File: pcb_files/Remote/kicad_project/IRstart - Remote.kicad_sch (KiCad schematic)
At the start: 44 parts, among them SW1 SW_DIP_x02, SW2 SW_DIP_x02, SW3 SW_DPDT_x2

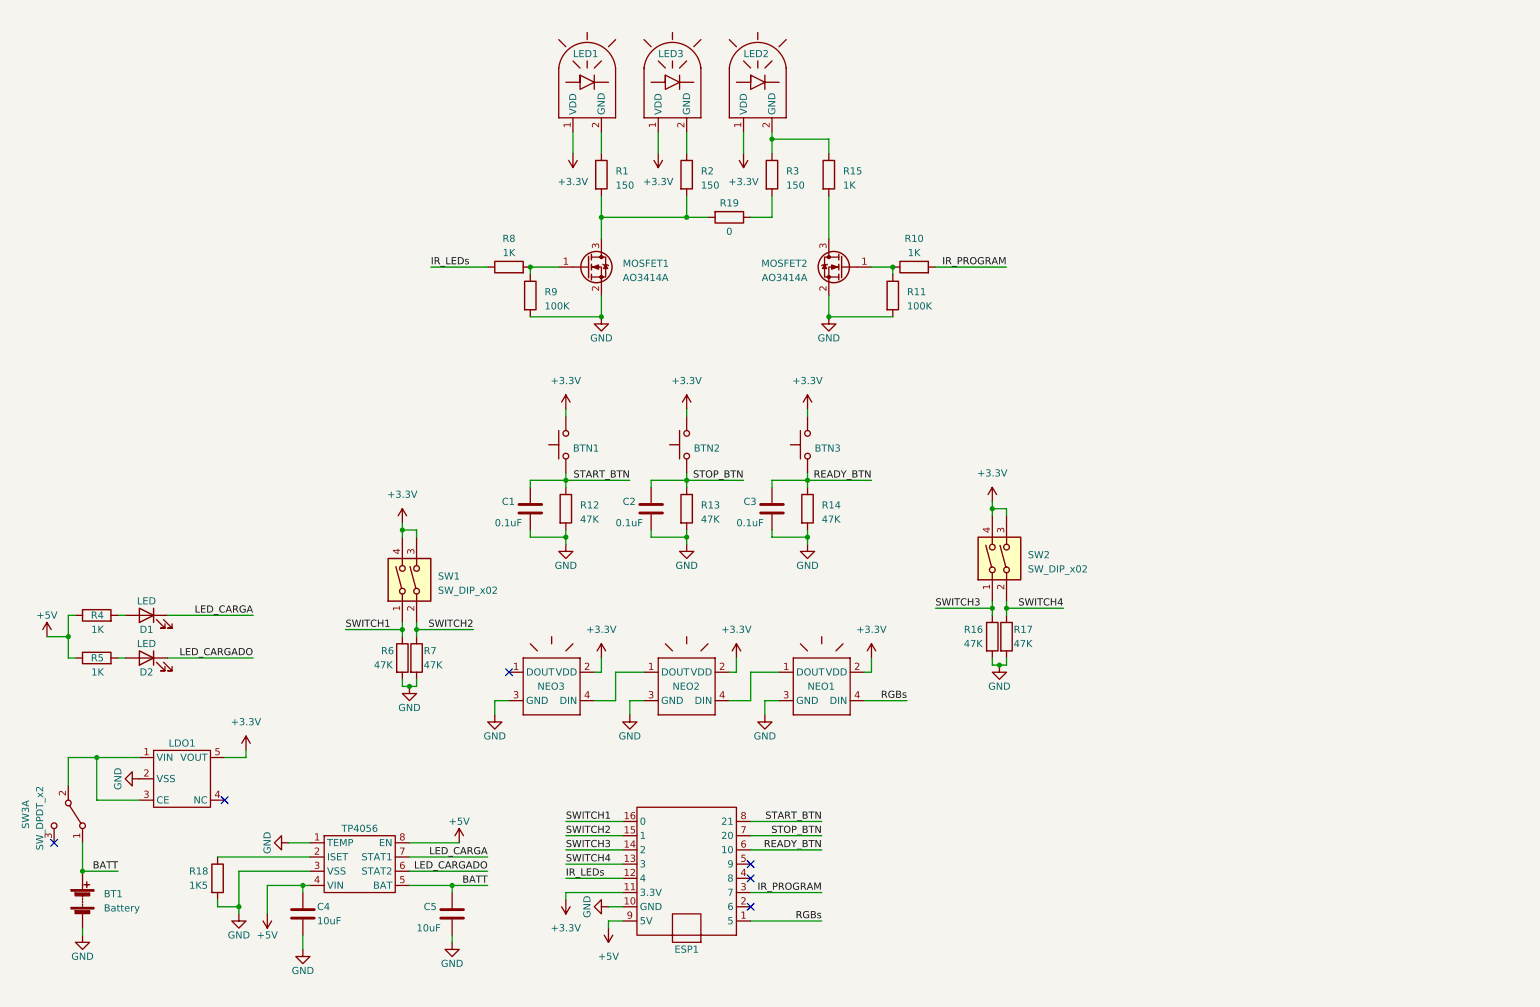
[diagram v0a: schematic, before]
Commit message: Añade gerbers de remote y adecenta el esquematico
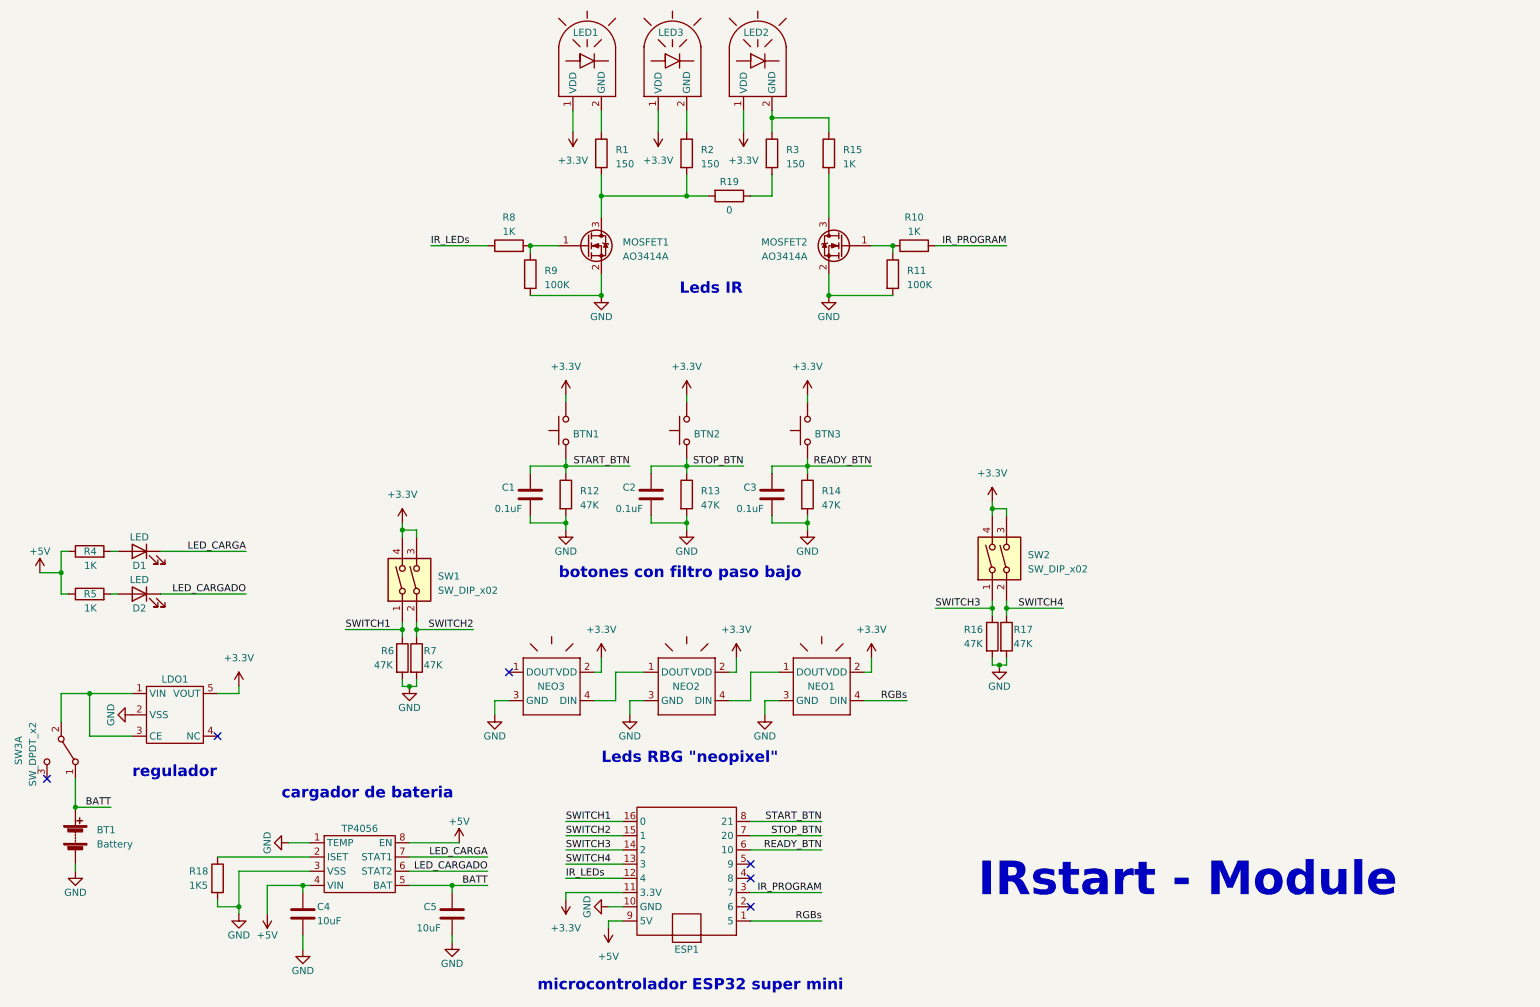
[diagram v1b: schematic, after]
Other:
- note added: "IRstart - Module"
- note added: "Leds IR"
- note added: "Leds RBG "neopixel""
- note added: "botones con filtro paso bajo"
- note added: "cargador de bateria"
- note added: "microcontrolador ESP32 super mini"
- note added: "regulador"
- moved on the sheet: BT1, BTN1, BTN2, BTN3, C1, C2, C3, D1, D2, LDO1, LED1, LED2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

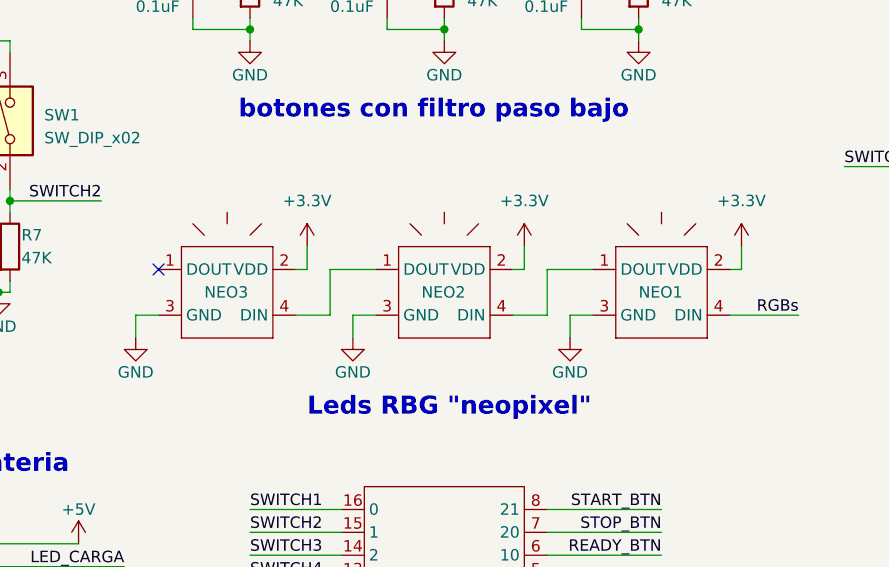
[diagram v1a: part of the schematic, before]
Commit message: Corrige leds RGB con huella incorrecta
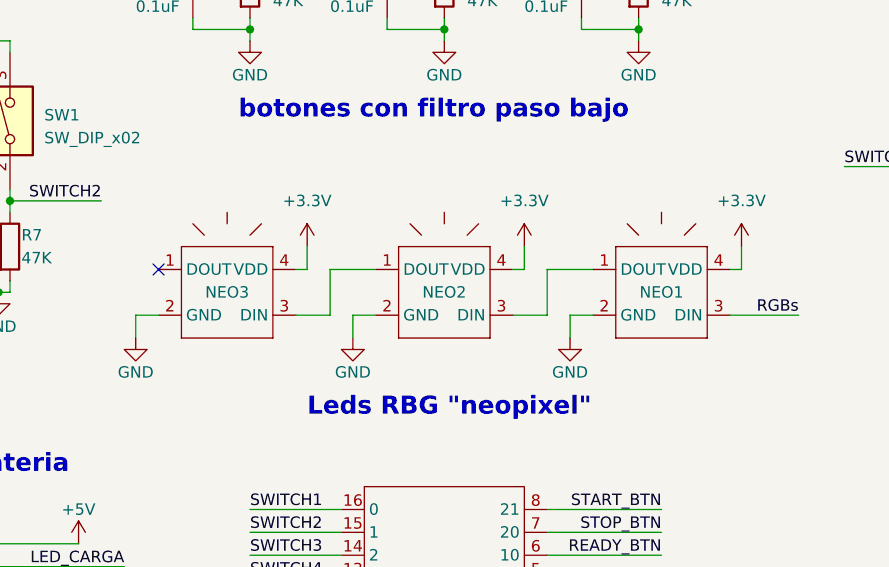
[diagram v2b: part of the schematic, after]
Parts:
- removed NEO1, NEO2, NEO3: ~, custom_footprints:LED_WS2812B_2.0x2.0mm, symbol custom_symbols:Led_5mm_WS2812D_
- added NEO1, NEO2, NEO3: ~, custom_footprints:LED_WS2812B_2.0x2.0mm, symbol custom_symbols:2020_Neopixel
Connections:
- net +3.3V: now also NEO1.4 (VDD), NEO2.4 (VDD), NEO3.4 (VDD)
- net GND: now also NEO1.2 (GND), NEO2.2 (GND), NEO3.2 (GND)
- net RGBs: now also NEO1.3 (DIN)
- new net: NEO1.1 (DOUT), NEO2.3 (DIN)
- new net: NEO2.1 (DOUT), NEO3.3 (DIN)
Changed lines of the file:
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@@
-    )
-  )
-  (symbol (lib_name "Led_5mm_WS2812D__1") (lib_id "custom_symbols:Led_5mm_WS2812D_") (at 139.7 143.51 0) (unit 1)
-    (in_bom yes) (on_board yes) (dnp no)
-    (property "Reference" "NEO2" (at 139.7 139.7 0)
-      (effects (font (size 1.27 1.27)) (justify left))
-    )
-    (property "Value" "~" (at 142.24 133.35 0)
-      (effects (font (size 1.27 1.27)))
-    )
-    (property "Footprint" "custom_footprints:LED_WS2812B_2.0x2.0mm" (at 142.24 147.32 0)
-      (effects (font (size 1.27 1.27)) hide)
-    )
-    (property "Datasheet" "" (at 139.7 143.51 0)
-      (effects (font (size 1.27 1.27)) hide)
-    )
-    (property "Aliexpress" "https://es.aliexpress.com/item/1005006449117605.html" (at 139.7 143.51 0)
-      (effects (font (size 1.27 1.27)) hide)
-    )
-    (pin "1")
-    (pin "2")
-    (pin "3")
-    (pin "4")
-    (instances
-      (project "IRstart - Remote"
-        (path "/1b43c11f-8fb9-449e-8aa5-32f4fc7dc112"
-          (reference "NEO2") (unit 1)
-        )
-      )
-      (project "PX-CORE"
-        (path "/b9d93021-acc9-4fa4-951b-65a13734b94e"
-          (reference "LED3") (unit 1)
-        )
-      )
     )
   )
@@
         (path "/b9d93021-acc9-4fa4-951b-65a13734b94e"
           (reference "#PWR018") (unit 1)
-        )
-      )
-    )
-  )
-  (symbol (lib_name "Led_5mm_WS2812D__1") (lib_id "custom_symbols:Led_5mm_WS2812D_") (at 163.83 143.51 0) (unit 1)
-    (in_bom yes) (on_board yes) (dnp no)
-    (property "Reference" "NEO1" (at 163.83 139.7 0)
-      (effects (font (size 1.27 1.27)) (justify left))
-    )
-    (property "Value" "~" (at 166.37 133.35 0)
-      (effects (font (size 1.27 1.27)))
-    )
-    (property "Footprint" "custom_footprints:LED_WS2812B_2.0x2.0mm" (at 166.37 147.32 0)
-      (effects (font (size 1.27 1.27)) hide)
-    )
-    (property "Datasheet" "" (at 163.83 143.51 0)
-      (effects (font (size 1.27 1.27)) hide)
-    )
-    (property "Aliexpress" "https://es.aliexpress.com/item/1005006449117605.html" (at 163.83 143.51 0)
-      (effects (font (size 1.27 1.27)) hide)
-    )
-    (pin "1")
-    (pin "2")
-    (pin "3")
-    (pin "4")
-    (instances
-      (project "IRstart - Remote"
-        (path "/1b43c11f-8fb9-449e-8aa5-32f4fc7dc112"
-          (reference "NEO1") (unit 1)
-        )
-      )
-      (project "PX-CORE"
-        (path "/b9d93021-acc9-4fa4-951b-65a13734b94e"
-          (reference "LED3") (unit 1)
         )
       )
@@
     )
   )
+  (symbol (lib_id "custom_symbols:2020_Neopixel") (at 163.83 143.51 0) (unit 1)
+    (in_bom yes) (on_board yes) (dnp no)
+    (property "Reference" "NEO1" (at 166.37 139.7 0)
+      (effects (font (size 1.27 1.27)))
+    )
+    (property "Value" "~" (at 166.37 133.35 0)
+      (effects (font (size 1.27 1.27)))
+    )
+    (property "Footprint" "custom_footprints:LED_WS2812B_2.0x2.0mm" (at 166.37 147.32 0)
+      (effects (font (size 1.27 1.27)) hide)
+    )
+    (property "Datasheet" "" (at 163.83 143.51 0)
+      (effects (font (size 1.27 1.27)) hide)
+    )
+    (property "Aliexpress" "https://es.aliexpress.com/item/1005006449117605.html" (at 163.83 143.51 0)
+      (effects (font (size 1.27 1.27)) hide)
+    )
+    (pin "1")
+    (pin "2")
+    (pin "3")
+    (pin "4")
+    (instances
+      (project "IRstart - Remote"
+        (path "/1b43c11f-8fb9-449e-8aa5-32f4fc7dc112"
+          (reference "NEO1") (unit 1)
+        )
+      )
+    )
+  )
   (symbol (lib_id "power:+5V") (at 67.31 180.34 180) (unit 1)
     (in_bom yes) (on_board yes) (dnp no)
@@
     )
   )
-  (symbol (lib_name "Led_5mm_WS2812D__1") (lib_id "custom_symbols:Led_5mm_WS2812D_") (at 115.57 143.51 0) (unit 1)
-    (in_bom yes) (on_board yes) (dnp no)
-    (property "Reference" "NEO3" (at 115.57 139.7 0)
-      (effects (font (size 1.27 1.27)) (justify left))
+  (symbol (lib_id "custom_symbols:2020_Neopixel") (at 115.57 143.51 0) (unit 1)
+    (in_bom yes) (on_board yes) (dnp no)
+    (property "Reference" "NEO3" (at 118.11 139.7 0)
+      (effects (font (size 1.27 1.27)))
     )
     (property "Value" "~" (at 118.11 133.35 0)
@@
         (path "/1b43c11f-8fb9-449e-8aa5-32f4fc7dc112"
           (reference "NEO3") (unit 1)
-        )
-      )
-      (project "PX-CORE"
-        (path "/b9d93021-acc9-4fa4-951b-65a13734b94e"
-          (reference "LED3") (unit 1)
         )
       )
@@
         )
       )
+    )
+  )
+  (symbol (lib_id "custom_symbols:2020_Neopixel") (at 139.7 143.51 0) (unit 1)
+    (in_bom yes) (on_board yes) (dnp no)
+    (property "Reference" "NEO2" (at 142.24 139.7 0)
+      (effects (font (size 1.27 1.27)))
+    )
+    (property "Value" "~" (at 142.24 133.35 0)
+      (effects (font (size 1.27 1.27)))
+    )
+    (property "Footprint" "custom_footprints:LED_WS2812B_2.0x2.0mm" (at 142.24 147.32 0)
+      (effects (font (size 1.27 1.27)) hide)
+    )
+    (property "Datasheet" "" (at 139.7 143.51 0)
+      (effects (font (size 1.27 1.27)) hide)
+    )
+    (property "Aliexpress" "https://es.aliexpress.com/item/1005006449117605.html" (at 139.7 143.51 0)
+      (effects (font (size 1.27 1.27)) hide)
+    )
+    (pin "1")
+    (pin "2")
+    (pin "3")
+    (pin "4")
+    (instances
+      (project "IRstart - Remote"
+        (path "/1b43c11f-8fb9-449e-8aa5-32f4fc7dc112"
+          (reference "NEO2") (unit 1)
+        )
+      )

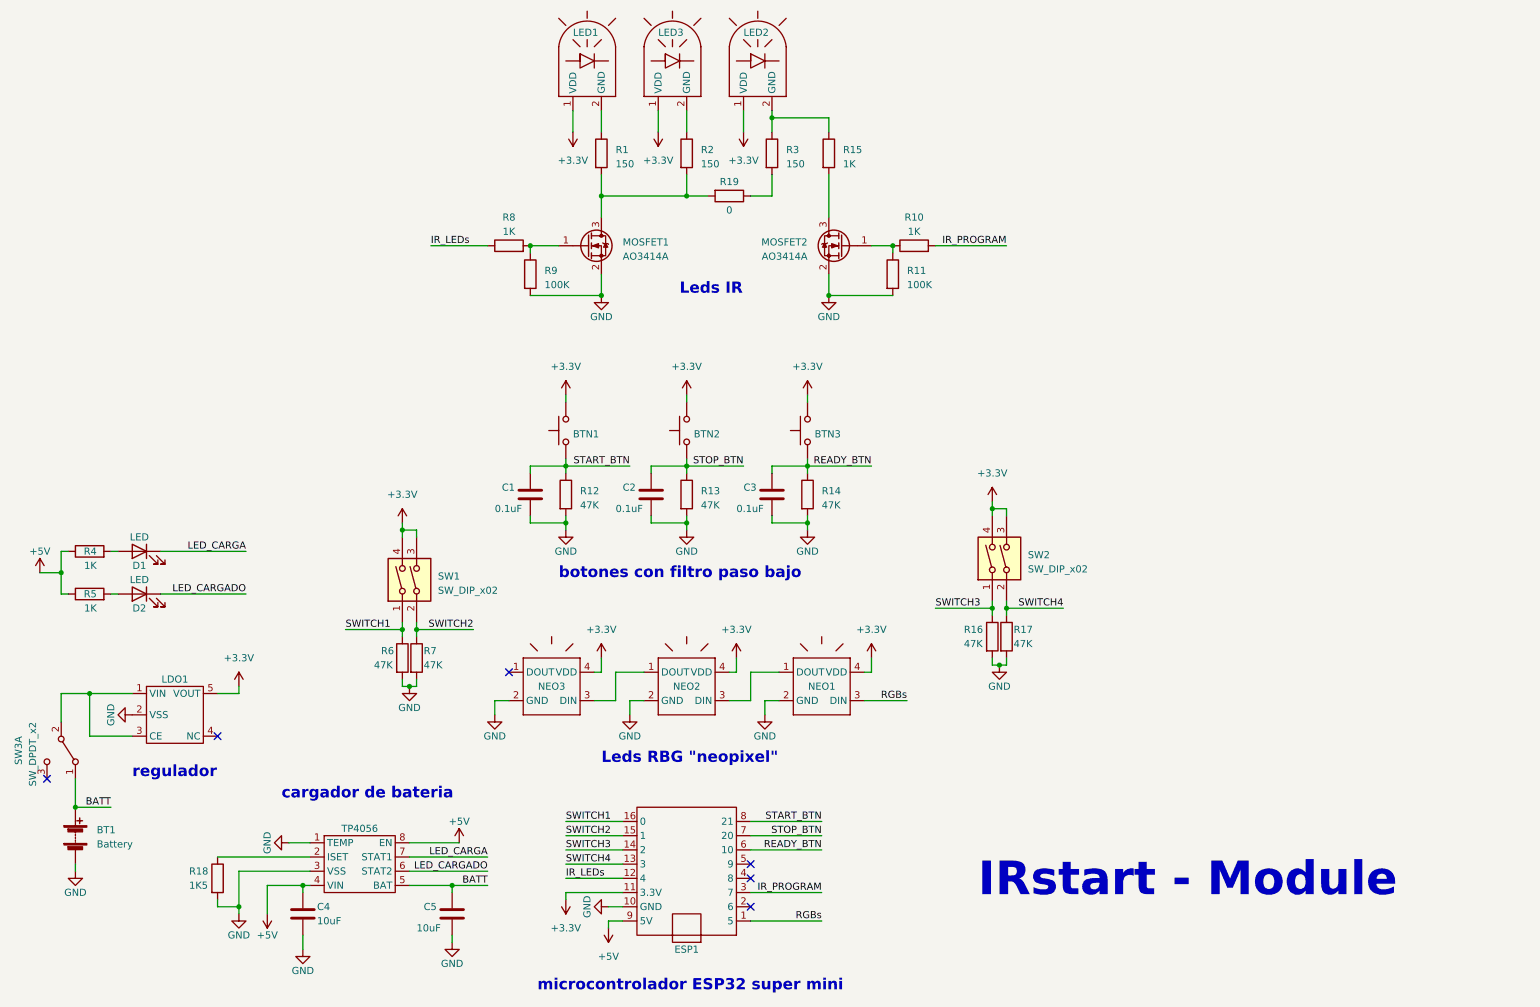
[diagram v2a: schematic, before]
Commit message: Crea la Rev.2 del mando añadiendo boton de modo y lectura de bateria
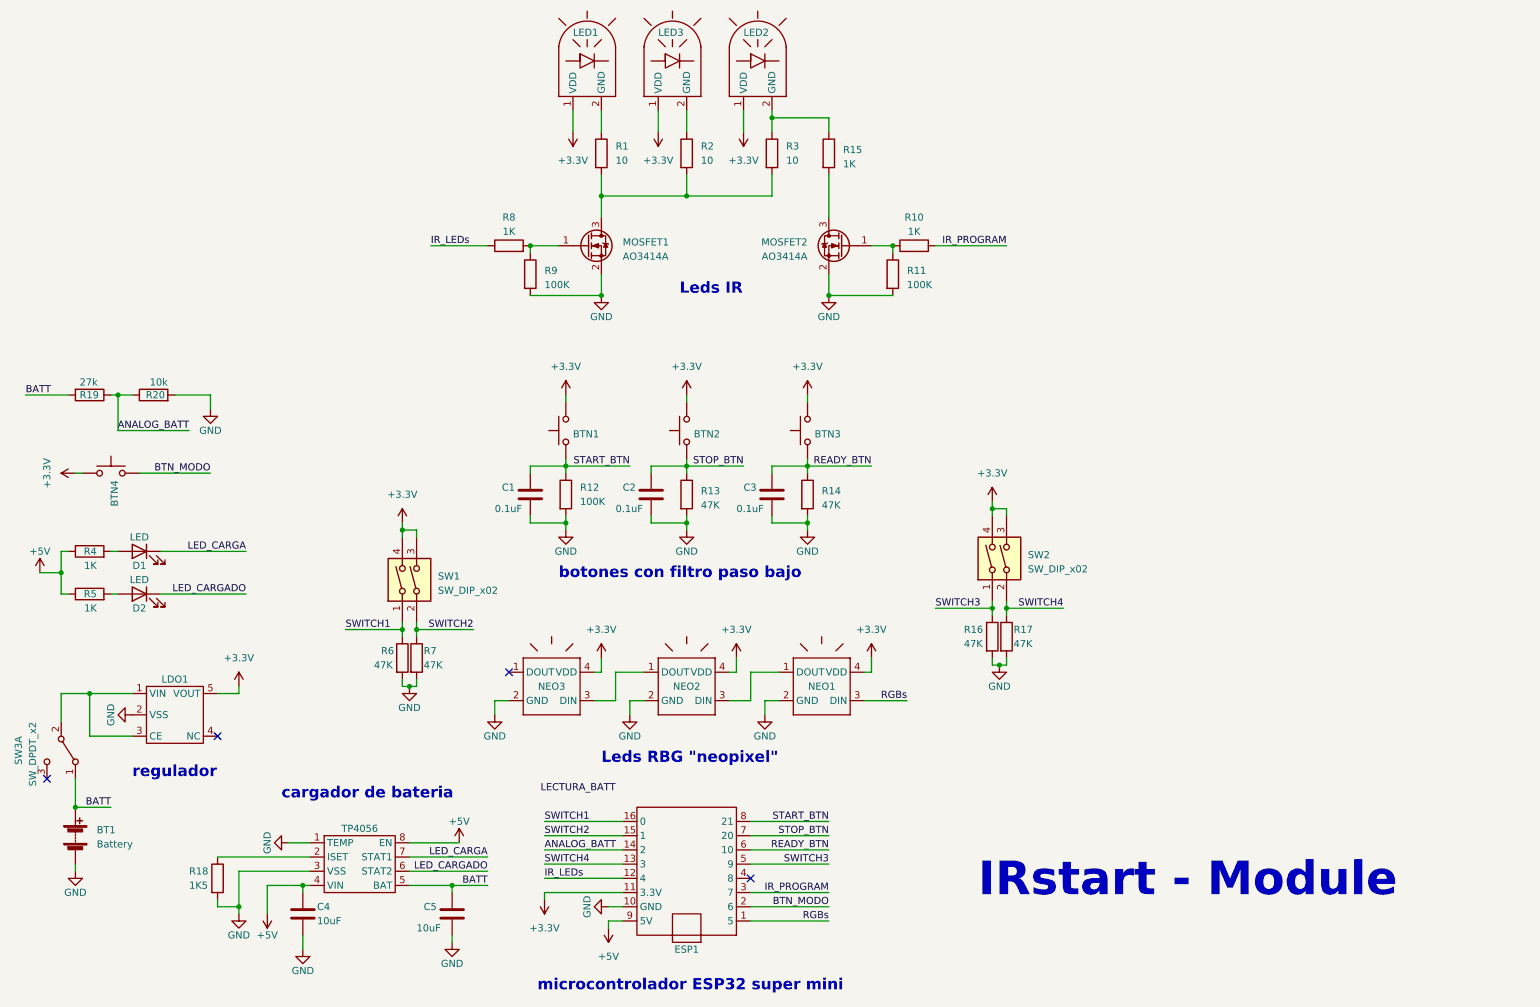
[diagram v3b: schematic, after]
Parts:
- added BTN4: ~, Button_Switch_SMD:SW_SPST_B3U-1000P, symbol custom_symbols:Button
- added R20: 10k, Resistor_SMD:R_0805_2012Metric_Pad1.20x1.40mm_HandSolder, symbol Device:R
- R1, R2, R3: value 150 -> 10
- R12: value 47K -> 100K
- R19: value 0 -> 27k
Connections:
- net +3.3V: now also BTN4.2
- net BATT: now also R19.2
- net GND: now also R20.2
- net SWITCH3: now also ESP1.5 (9); no longer ESP1.14 (2)
- net at R3.2: now also MOSFET1.3 (D), R1.2, R2.2; no longer R19.1
- net BTN_MODO: now reaches ESP1.2 (6)
- net BTN_MODO: now also BTN4.1
- new net ANALOG_BATT: ESP1.14 (2), R19.1, R20.1
- no-connect marks 6 -> 4
